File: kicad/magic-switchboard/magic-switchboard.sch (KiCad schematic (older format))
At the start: 22 parts, among them J1 AVR-ISP-6, Q1 BC547, Q2 BC547, Q3 BC547, Q4 BC547, SW1 MTS-103, SW2 MTS-103, SW3 MTS-103, SW4 MTS-103, U1 ATtiny2313A-PU, U2 5V Boost

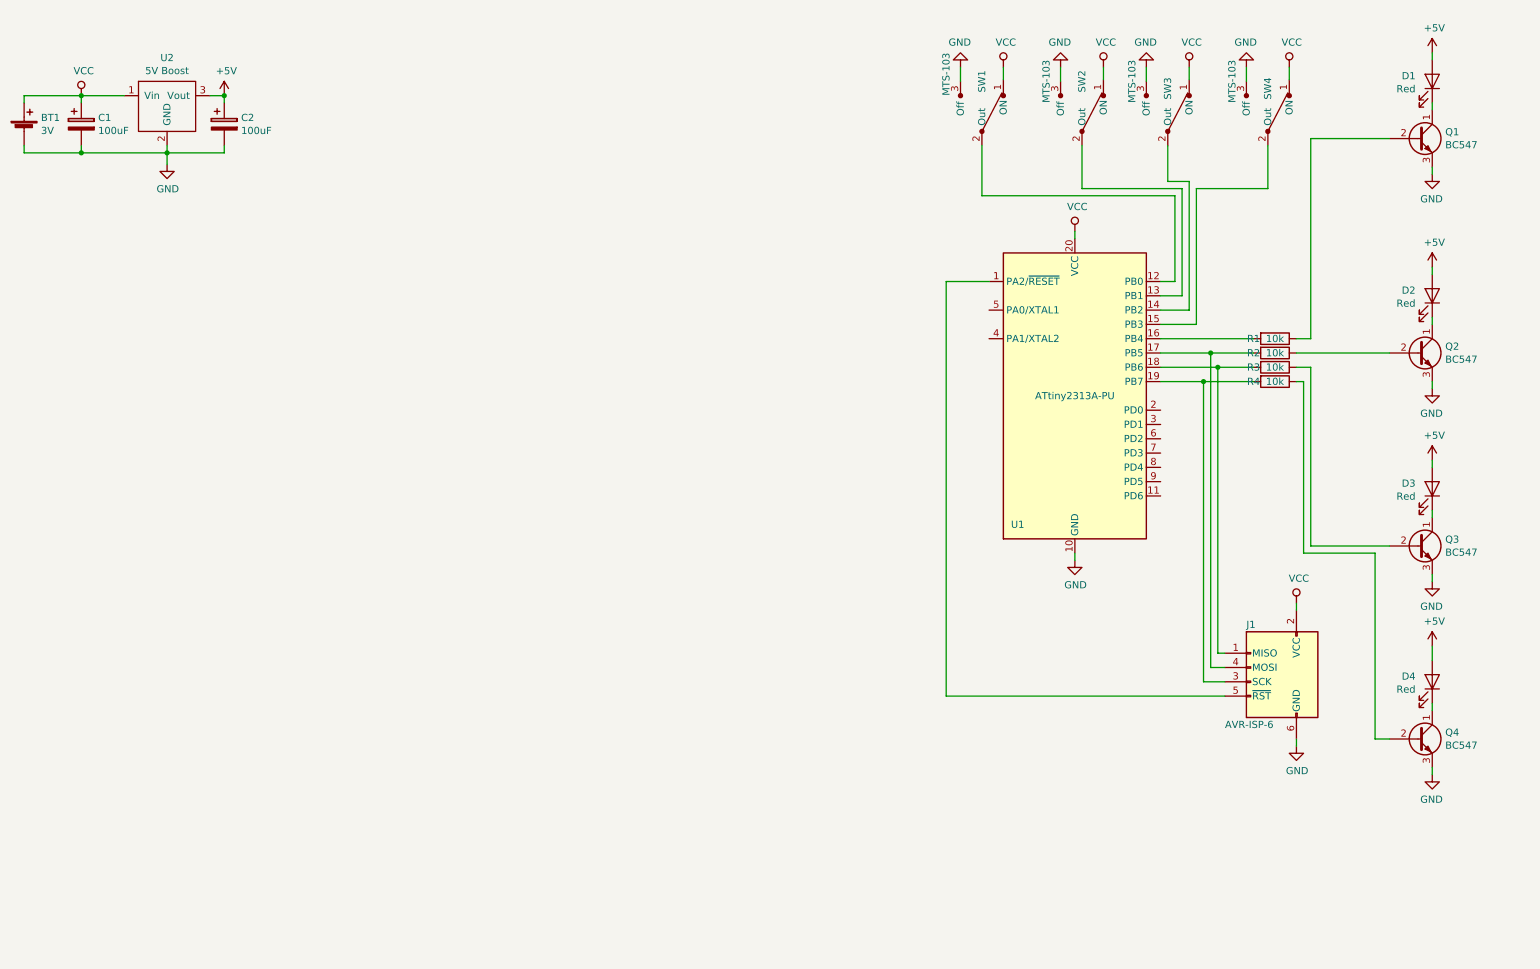
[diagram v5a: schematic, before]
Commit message: aufgeräumt für v4 (attiny4313)
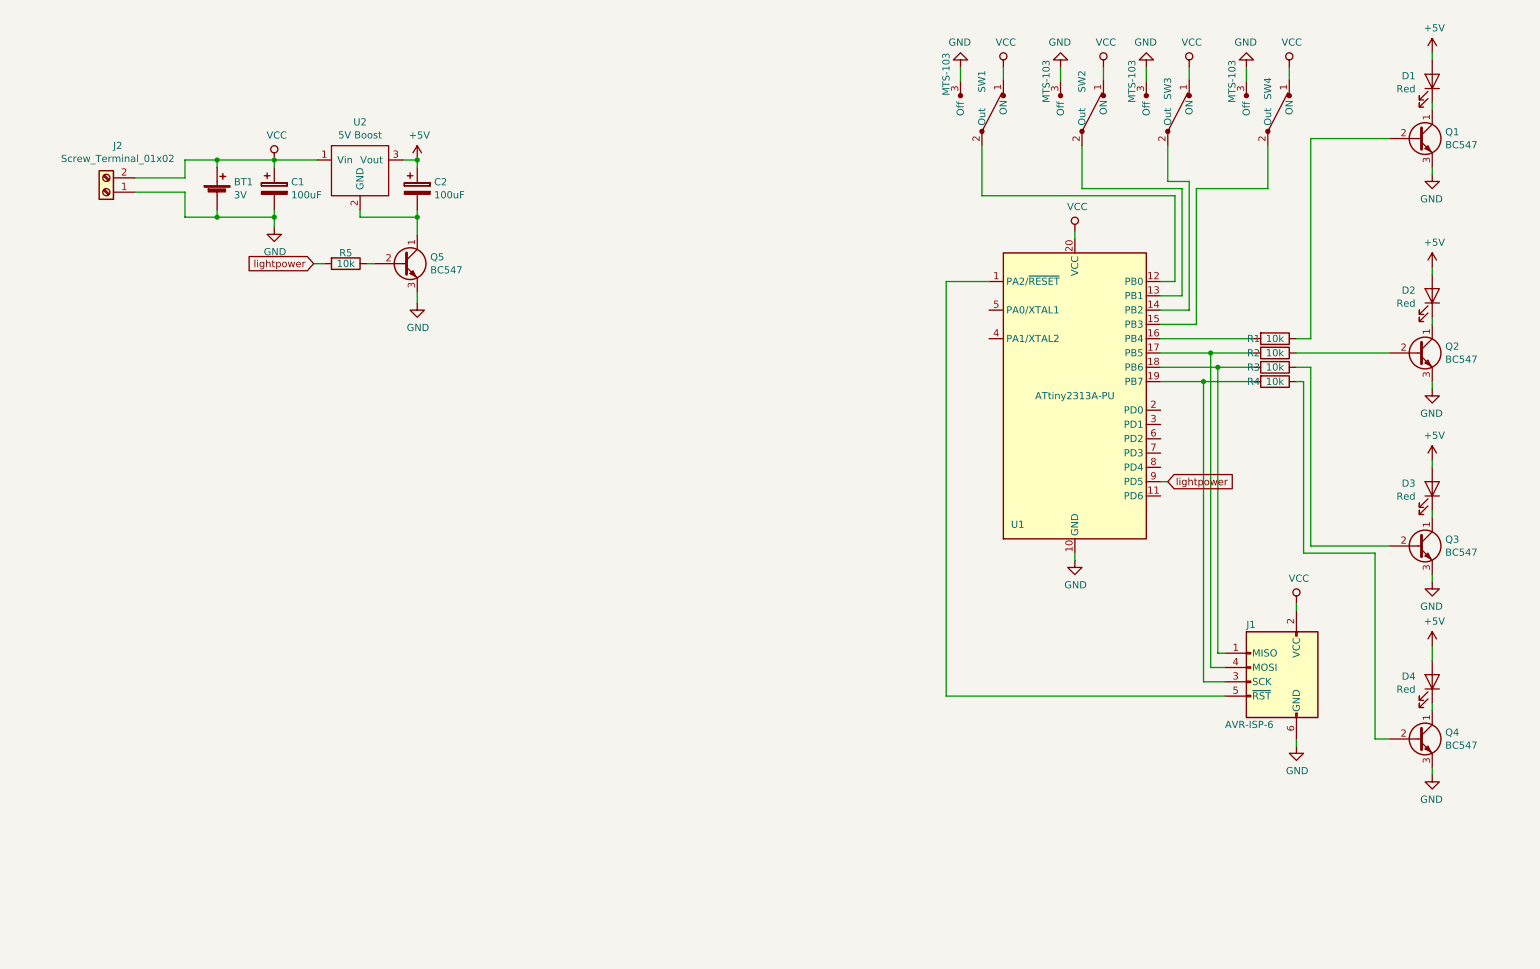
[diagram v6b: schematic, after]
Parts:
- added J2: Screw_Terminal_01x02, switchboard:ScrewTerminal1x2, symbol Connector:Screw_Terminal_01x02
- added Q5: BC547, Package_TO_SOT_THT:TO-92_Inline, symbol Transistor_BJT:BC547
- added R5: 10k, switchboard:Resistor, symbol Device:R
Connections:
- net GND: now also J2.1 (Pin_1), Q5.3 (E); no longer C2.2, U2.2 (GND)
- net VCC: now also J2.2 (Pin_2)
- net lightpower: now reaches U1.9 (PD5)
- net lightpower: now also R5.2
- new net: C2.2, Q5.1 (C), U2.2 (GND)
- new net: Q5.2 (B), R5.1
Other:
- moved on the sheet: BT1, C1, C2, U2
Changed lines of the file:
@@
 Title "Magic Switchboard"
 Date "2018-12-31"
-Rev "r2"
+Rev "r4"
 Comp "magierdinge.de"
-Comment1 ""
+Comment1 "attiny2313 version"
 Comment2 ""
 Comment3 ""
@@
 L Device:Battery_Cell BT1
 U 1 1 5C2A4986
-P 750 1350
-F 0 "BT1" H 868 1446 50  0000 L CNN
-F 1 "3V" H 868 1355 50  0000 L CNN
-F 2 "switchboard:BatteryHolder_Keystone_3009_1x2450" V 750 1410 50  0001 C CNN
-F 3 "~" V 750 1410 50  0001 C CNN
-	1    750  1350
+P 2100 1800
+F 0 "BT1" H 2218 1896 50  0000 L CNN
+F 1 "3V" H 2218 1805 50  0000 L CNN
+F 2 "switchboard:BatteryHolder_Keystone_3009_1x2450" V 2100 1860 50  0001 C CNN
+F 3 "~" V 2100 1860 50  0001 C CNN
+	1    2100 1800
 	1    0    0    -1
 $EndComp
@@
 L power:VCC #PWR04
 U 1 1 5C2A6172
-P 1150 1100
-F 0 "#PWR04" H 1150 950 50  0001 C CNN
-F 1 "VCC" H 1167 1273 50  0000 C CNN
-F 2 "" H 1150 1100 50  0001 C CNN
-F 3 "" H 1150 1100 50  0001 C CNN
-	1    1150 1100
+P 2500 1550
+F 0 "#PWR04" H 2500 1400 50  0001 C CNN
+F 1 "VCC" H 2517 1723 50  0000 C CNN
+F 2 "" H 2500 1550 50  0001 C CNN
+F 3 "" H 2500 1550 50  0001 C CNN
+	1    2500 1550
 	1    0    0    -1
 $EndComp
@@
 L Device:CP C1
 U 1 1 5C2CDA79
-P 1150 1300
-F 0 "C1" H 1268 1346 50  0000 L CNN
-F 1 "100uF" H 1268 1255 50  0000 L CNN
-F 2 "switchboard:CP_Radial_D6.3mm_P2.50mm" H 1188 1150 50  0001 C CNN
-F 3 "~" H 1150 1300 50  0001 C CNN
-	1    1150 1300
+P 2500 1750
+F 0 "C1" H 2618 1796 50  0000 L CNN
+F 1 "100uF" H 2618 1705 50  0000 L CNN
+F 2 "switchboard:CP_Radial_D6.3mm_P2.50mm" H 2538 1600 50  0001 C CNN
+F 3 "~" H 2500 1750 50  0001 C CNN
+	1    2500 1750
 	1    0    0    -1
 $EndComp
@@
 L Device:CP C2
 U 1 1 5C2D5FC7
-P 2150 1300
-F 0 "C2" H 2268 1346 50  0000 L CNN
-F 1 "100uF" H 2268 1255 50  0000 L CNN
-F 2 "switchboard:CP_Radial_D6.3mm_P2.50mm" H 2188 1150 50  0001 C CNN
-F 3 "~" H 2150 1300 50  0001 C CNN
-	1    2150 1300
+P 3500 1750
+F 0 "C2" H 3618 1796 50  0000 L CNN
+F 1 "100uF" H 3618 1705 50  0000 L CNN
+F 2 "switchboard:CP_Radial_D6.3mm_P2.50mm" H 3538 1600 50  0001 C CNN
+F 3 "~" H 3500 1750 50  0001 C CNN
+	1    3500 1750
 	1    0    0    -1
 $EndComp
@@
 L switchboard:BoostConverter U2
 U 1 1 5C4DCF30
-P 1750 1100
-F 0 "U2" H 1750 1365 50  0000 C CNN
-F 1 "5V Boost" H 1750 1274 50  0000 C CNN
-F 2 "switchboard:BoostConverter3Pin" H 1750 1100 50  0001 C CNN
-F 3 "" H 1750 1100 50  0001 C CNN
-	1    1750 1100
+P 3100 1550
+F 0 "U2" H 3100 1815 50  0000 C CNN
+F 1 "5V Boost" H 3100 1724 50  0000 C CNN
+F 2 "switchboard:BoostConverter3Pin" H 3100 1550 50  0001 C CNN
+F 3 "" H 3100 1550 50  0001 C CNN
+	1    3100 1550
 	1    0    0    -1
 $EndComp
@@
 L power:GND #PWR028
 U 1 1 5C4E17B4
-P 1750 1580
-F 0 "#PWR028" H 1750 1330 50  0001 C CNN
-F 1 "GND" H 1755 1407 50  0000 C CNN
-F 2 "" H 1750 1580 50  0001 C CNN
-F 3 "" H 1750 1580 50  0001 C CNN
-	1    1750 1580
+P 2500 2020
+F 0 "#PWR028" H 2500 1770 50  0001 C CNN
+F 1 "GND" H 2505 1847 50  0000 C CNN
+F 2 "" H 2500 2020 50  0001 C CNN
+F 3 "" H 2500 2020 50  0001 C CNN
+	1    2500 2020
 	1    0    0    -1
 $EndComp
@@
 L power:+5V #PWR01
 U 1 1 5C504B49
-P 2150 1100
-F 0 "#PWR01" H 2150 950 50  0001 C CNN
-F 1 "+5V" H 2165 1273 50  0000 C CNN
-F 2 "" H 2150 1100 50  0001 C CNN
-F 3 "" H 2150 1100 50  0001 C CNN
-	1    2150 1100
-	1    0    0    -1
-$EndComp
-Wire Wire Line
-	1750 1500 1750 1450
-Wire Wire Line
-	1450 1100 1150 1100
-Wire Wire Line
-	1150 1100 1150 1150
-Wire Wire Line
-	1150 1100 750  1100
-Wire Wire Line
-	750  1100 750  1150
-Connection ~ 1150 1100
-Wire Wire Line
-	750  1450 750  1500
-Wire Wire Line
-	750  1500 1150 1500
-Wire Wire Line
-	1150 1500 1150 1450
-Wire Wire Line
-	1150 1500 1750 1500
-Connection ~ 1150 1500
-Connection ~ 1750 1500
-Wire Wire Line
-	1750 1500 2150 1500
-Wire Wire Line
-	2150 1500 2150 1450
-Wire Wire Line
-	2150 1150 2150 1100
-Wire Wire Line
-	2150 1100 2050 1100
-Connection ~ 2150 1100
+P 3500 1550
+F 0 "#PWR01" H 3500 1400 50  0001 C CNN
+F 1 "+5V" H 3515 1723 50  0000 C CNN
+F 2 "" H 3500 1550 50  0001 C CNN
+F 3 "" H 3500 1550 50  0001 C CNN
+	1    3500 1550
+	1    0    0    -1
+$EndComp
+Wire Wire Line
+	2800 1550 2500 1550
+Wire Wire Line
+	2500 1550 2500 1600
+Wire Wire Line
+	2500 1550 2100 1550
+Wire Wire Line
+	2100 1550 2100 1600
+Connection ~ 2500 1550
+Wire Wire Line
+	2100 1900 2100 1950
+Wire Wire Line
+	2100 1950 2500 1950
+Wire Wire Line
+	2500 1950 2500 1900
+Wire Wire Line
+	3500 1950 3500 1900
+Wire Wire Line
+	3500 1600 3500 1550
+Wire Wire Line
+	3500 1550 3400 1550
+Connection ~ 3500 1550
 $Comp
 L power:GND #PWR03
@@
 	10600 3700 10600 3650
 Wire Wire Line
-	1750 1500 1750 1580
+	2500 2020 2500 1950
+Connection ~ 2500 1950
+Wire Wire Line
+	3500 1950 3100 1950
+Wire Wire Line
+	3100 1950 3100 1900
+$Comp
+L Transistor_BJT:BC547 Q5
+U 1 1 5C4E6680
+P 3400 2275
+F 0 "Q5" H 3591 2321 50  0000 L CNN
+F 1 "BC547" H 3591 2230 50  0000 L CNN
+F 2 "Package_TO_SOT_THT:TO-92_Inline" H 3600 2200 50  0001 L CIN
+F 3 "http://www.fairchildsemi.com/ds/BC/BC547.pdf" H 3400 2275 50  0001 L CNN
+	1    3400 2275
+	1    0    0    -1
+$EndComp
+Wire Wire Line
+	3500 2075 3500 1950
+Connection ~ 3500 1950
+$Comp
+L power:GND #PWR018
+U 1 1 5C4E864A
+P 3500 2550
+F 0 "#PWR018" H 3500 2300 50  0001 C CNN
+F 1 "GND" H 3505 2377 50  0000 C CNN
+F 2 "" H 3500 2550 50  0001 C CNN
+F 3 "" H 3500 2550 50  0001 C CNN
+	1    3500 2550
+	1    0    0    -1
+$EndComp
+Wire Wire Line
+	3500 2550 3500 2475
+Text GLabel 8750 3800 2    50   Input ~ 0
+lightpower
+Wire Wire Line
+	8750 3800 8700 3800
+Text GLabel 2775 2275 0    50   Input ~ 0
+lightpower
+Wire Wire Line
+	3150 2275 3200 2275
+$Comp
+L Device:R R5
+U 1 1 5C4EFD8C
+P 3000 2275
+F 0 "R5" V 2925 2275 50  0000 C CNN
+F 1 "10k" V 3000 2275 50  0000 C CNN
+F 2 "switchboard:Resistor" V 2930 2275 50  0001 C CNN
+F 3 "~" H 3000 2275 50  0001 C CNN
+	1    3000 2275
+	0    1    1    0
+$EndComp
+Wire Wire Line
+	2775 2275 2850 2275
+$Comp
+L Connector:Screw_Terminal_01x02 J2
+U 1 1 5C4F2DCC
+P 1325 1775
+F 0 "J2" H 1245 1450 50  0000 C CNN
+F 1 "Screw_Terminal_01x02" H 1245 1541 50  0000 C CNN
+F 2 "switchboard:ScrewTerminal1x2" H 1325 1775 50  0001 C CNN
+F 3 "~" H 1325 1775 50  0001 C CNN
+	1    1325 1775
+	-1   0    0    1
+$EndComp
+Wire Wire Line
+	1525 1675 1875 1675
+Wire Wire Line
+	1875 1675 1875 1550
+Wire Wire Line
+	1875 1550 2100 1550
+Connection ~ 2100 1550
+Wire Wire Line
+	2100 1950 1875 1950
+Wire Wire Line
+	1875 1950 1875 1775
+Wire Wire Line
+	1875 1775 1525 1775
+Connection ~ 2100 1950
 $EndSCHEMATC

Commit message: Zwischenboden Bohrplan
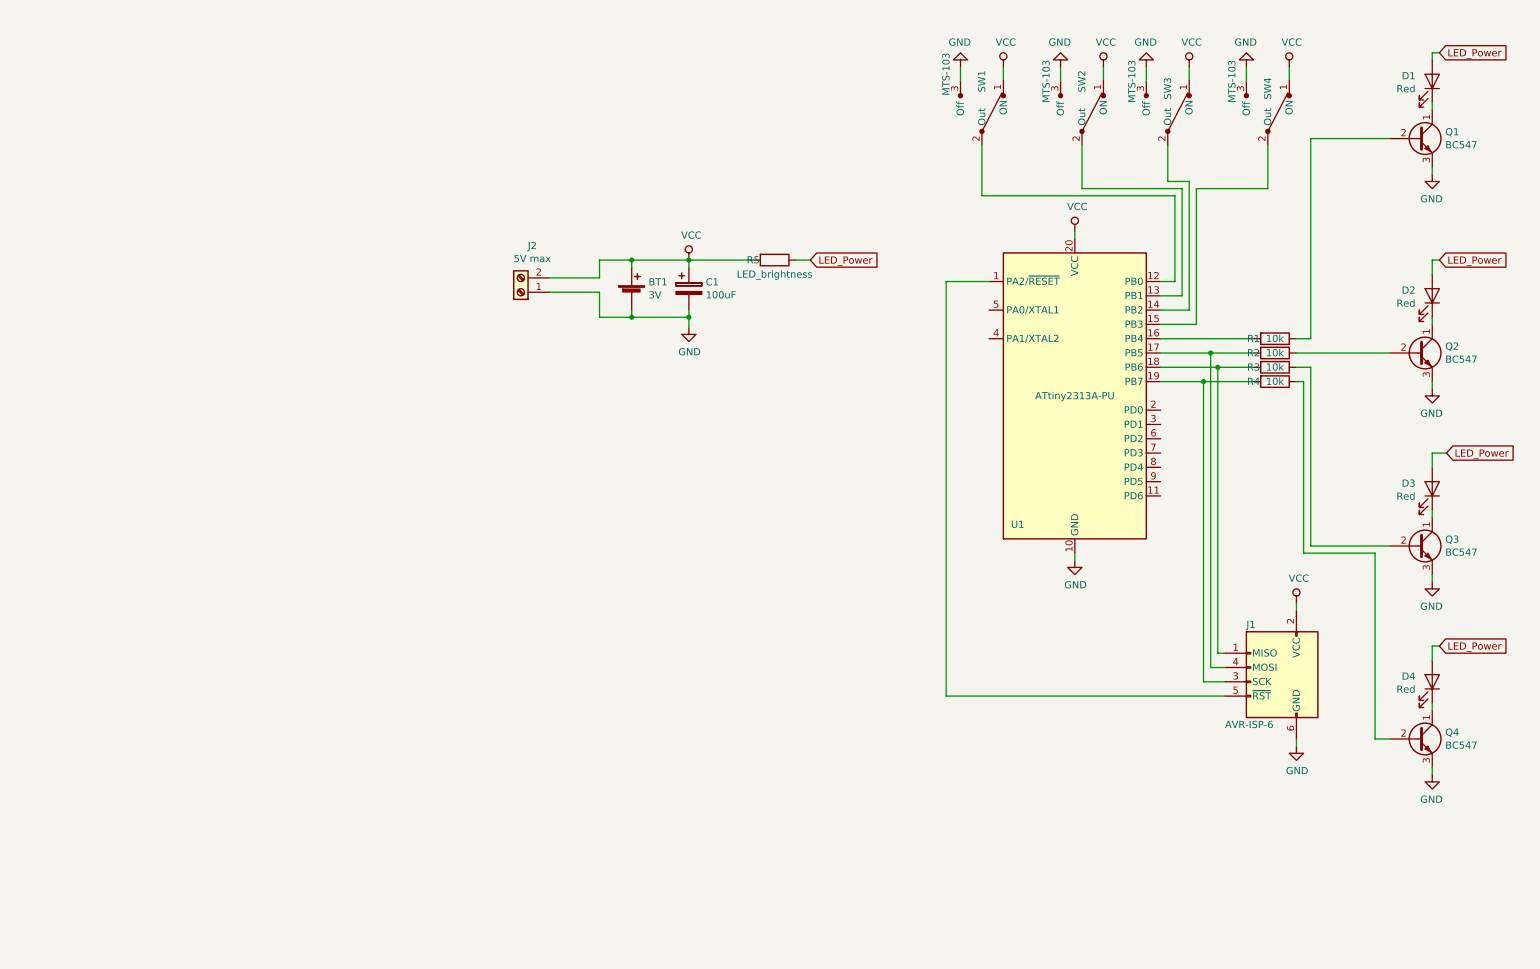
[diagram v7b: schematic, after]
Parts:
- removed C2: 100uF, switchboard:CP_Radial_D6.3mm_P2.50mm, symbol Device:CP
- removed Q5: BC547, Package_TO_SOT_THT:TO-92_Inline, symbol Transistor_BJT:BC547
- removed U2: 5V Boost, switchboard:BoostConverter3Pin, symbol switchboard:BoostConverter
- J2: value Screw_Terminal_01x02 -> 5V max
- Q1, Q2, Q3, Q4: footprint Package_TO_SOT_THT:TO-92_Inline -> switchboard:BC547
- R5: value 10k -> LED_brightness
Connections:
- net +5V is gone; now on net LED_Power: D1.2 (A), D2.2 (A), D3.2 (A), D4.2 (A)
- net VCC: now also R5.2
- net LED_Power: now reaches R5.1
- net lightpower: no longer names the net of U1.9 (PD5)
- net lightpower: no longer R5.2
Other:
- moved on the sheet: BT1, C1, J2
